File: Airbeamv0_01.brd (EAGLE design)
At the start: 91.4 x 74.3 mm, 89 parts

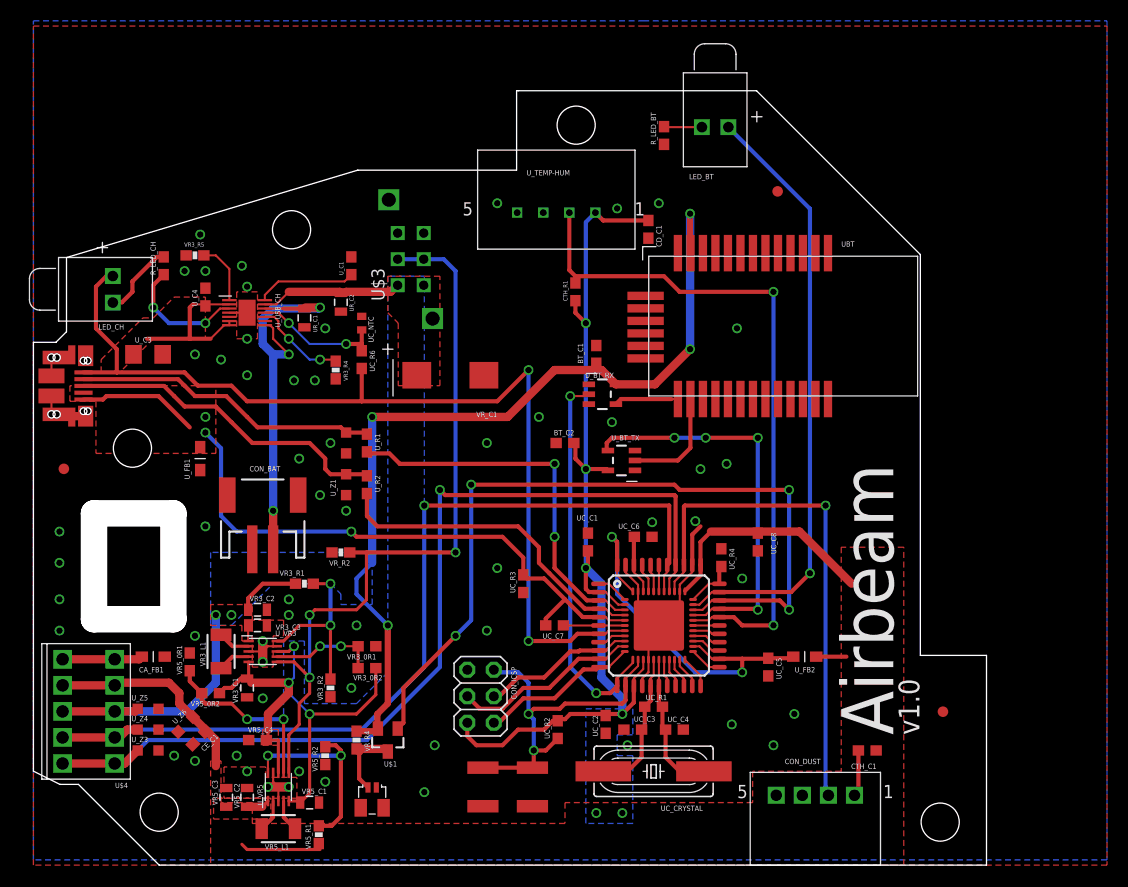
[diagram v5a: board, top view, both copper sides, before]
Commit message: updated bom, added ferrite bead
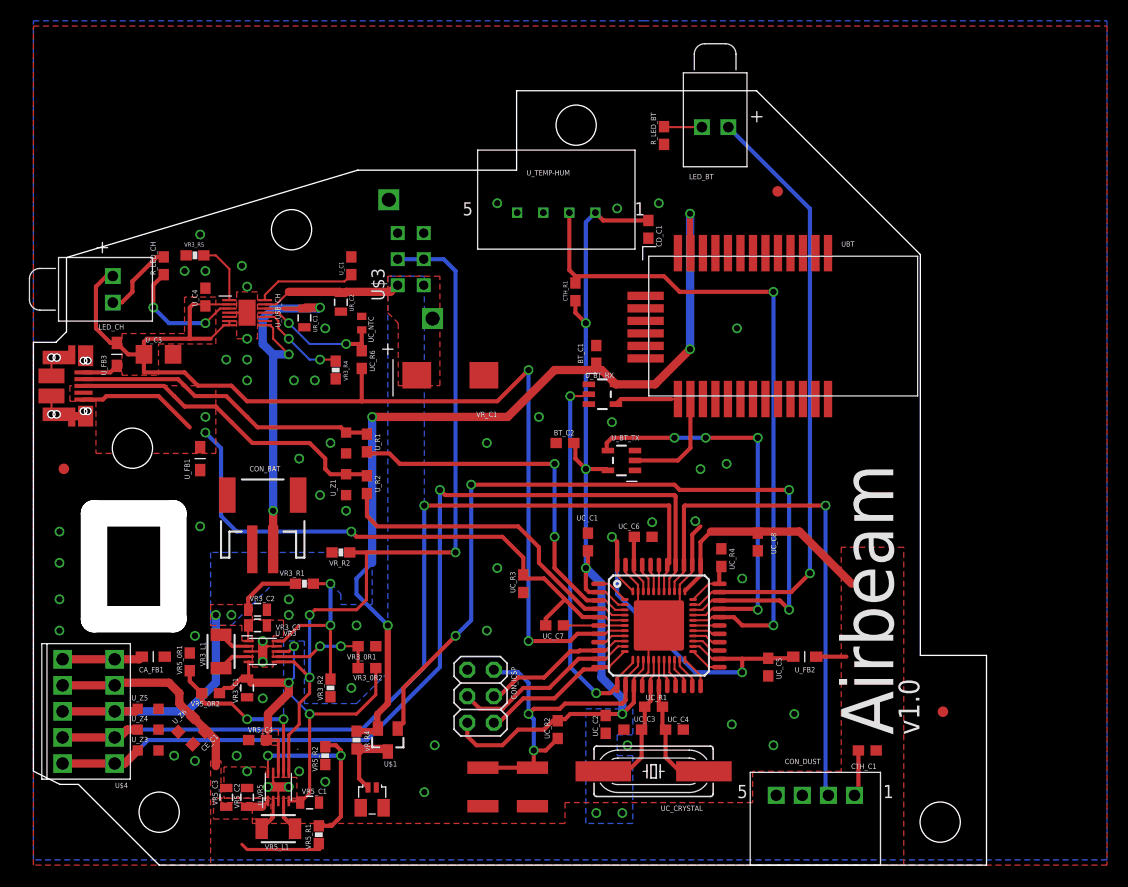
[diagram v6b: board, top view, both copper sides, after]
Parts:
- added U_FB3: FERITE_BEAD, Airbeam:U_FB1
- moved U_C3 1.00 mm to (12.0, 49.0)
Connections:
- new net VUSB: ATMEGA32U4-T.7, LED_CH.ANODE, UC_R6.2, U_C3.1, U_C4.1, U_FB3.P$2, U_MEGA32U-Q.7, U_USB_CH.P$2, U_USB_CH.P$6, U_USB_CH.P$7
- net XUSB: now also U_FB3.P$1; no longer ATMEGA32U4-T.7, LED_CH.ANODE, UC_R6.2, U_C3.1, U_C4.1, U_MEGA32U-Q.7, U_USB_CH.P$2, U_USB_CH.P$6, U_USB_CH.P$7
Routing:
- net VUSB: track 0.00 -> 108.9 mm, vias 0 -> 2
- net XUSB: track 110.8 -> 3.45 mm, vias 2 -> 0
- added copper zone on layer 1, net VUSB
- removed copper zone on layer 1, net XUSB
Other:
- outline, holes or cut-outs redrawn

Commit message: updating for ordering
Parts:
- RESET_SWITCH: value SWITCH -> DNP
- U_FANM: value MOSFET-N -> DNP
- renumbered U$1 to U_FANM, U$4 to CON_EXTERN
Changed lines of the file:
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@@
 <wire x1="5.768" y1="42.074" x2="5.768" y2="44.019" width="0.025" layer="49"/>
 <wire x1="5.768" y1="47.929" x2="5.768" y2="49.874" width="0.025" layer="49"/>
-<wire x1="46.53788125" y1="74.295" x2="46.53788125" y2="66.675" width="0.025" layer="49"/>
 <wire x1="3.358" y1="42.074" x2="4.058" y2="42.074" width="0.025" layer="49"/>
 <wire x1="4.308" y1="42.074" x2="5.768" y2="42.074" width="0.025" layer="49"/>
@@
 <wire x1="5.768" y1="49.874" x2="4.308" y2="49.874" width="0.025" layer="49"/>
 <wire x1="4.058" y1="49.874" x2="3.358" y2="49.874" width="0.025" layer="49"/>
-<wire x1="46.355" y1="66.675" x2="46.53788125" y2="66.675" width="0.025" layer="49"/>
 <wire x1="69.37761875" y1="74.295" x2="46.355" y2="74.295" width="0.025" layer="20"/>
 <circle x="9.525" y="40.005" radius="1.8288" width="0.025" layer="49"/>
@@
 <attribute name="NAME" x="45.847" y="19.021" size="0.508" layer="25" font="vector" ratio="27" rot="R270"/>
 <attribute name="PARTNO" value="67997-206HLF " x="42.9" y="16.2" size="1.778" layer="27" rot="R90" display="off"/>
-<attribute name="DNP" x="42.9" y="16.2" size="1.778" layer="27" rot="R90" display="off"/>
 </element>
 <element name="FID1" library="SmartPrj" package="FIDUCIA-MOUNT" value="FIDUCIALMOUNT" x="2.92" y="38.02" smashed="yes">
@@
 </element>
 <element name="ATMEGA32U4-T" library="SmartPrj" package="TQFP44-PAD" value="ATMEGA32U4-XUAU" x="60.01" y="22.99" smashed="yes">
-<attribute name="PARTNO" value="AtMega32U4-XUAU" x="60.01" y="22.99" size="1.778" layer="27" display="off"/>
+<attribute name="PARTNO" value="ATMEGA32U4-AU" x="60.01" y="22.99" size="1.778" layer="27" display="off"/>
 </element>
 <element name="UBT" library="Airbeam" package="BT_NVC-MDCS42A" value="BT-NVC-MDCS42A" x="76.2325" y="51.715" smashed="yes" rot="R270">
@@
 <attribute name="NAME" x="17.889" y="15.738" size="0.508" layer="25" font="vector" ratio="27" rot="R180"/>
 </element>
-<element name="RESET_SWITCH" library="Airbeam" package="SWITCH_TACTILE" value="SWITCH" x="45.5" y="7.5" smashed="yes" rot="R180">
+<element name="RESET_SWITCH" library="Airbeam" package="SWITCH_TACTILE" value="DNP" x="45.5" y="7.5" smashed="yes" rot="R180">
 <attribute name="PARTNO" value="TL3315NF250Q" x="45.5" y="7.5" size="1.778" layer="27" rot="R180" display="off"/>
 <attribute name="DNP" x="45.5" y="7.5" size="1.778" layer="27" rot="R180" display="off"/>
@@
 <attribute name="NAME" x="75" y="19" size="0.508" layer="25" ratio="27" rot="R180"/>
 </element>
-<element name="U$1" library="Airbeam" package="SOT23" value="MOSFET-N" x="34" y="12" smashed="yes" rot="R180">
+<element name="U_FANM" library="Airbeam" package="SOT23" value="DNP" x="34" y="12" smashed="yes" rot="R180">
 <attribute name="PARTNO" value="NDS331N" x="34" y="12" size="1.778" layer="27" rot="R180" display="off"/>
 <attribute name="NAME" x="34.889" y="9.968" size="0.508" layer="25" ratio="27" rot="R180"/>
@@
 <attribute name="PARTNO" value="RC0603JR-0710KL" x="52" y="55" size="0.508" layer="27" ratio="27" rot="R90" display="off"/>
 </element>
-<element name="U$4" library="Airbeam" package="TBLOCK_5" value="TBLOCK_5" x="5.3" y="14.75" locked="yes" rot="R90"/>
+<element name="CON_EXTERN" library="Airbeam" package="TBLOCK_5" value="TBLOCK_5" x="5.3" y="14.75" locked="yes" rot="R90">
+<attribute name="PARTNO" value="1770911" x="5.3" y="14.75" size="1.778" layer="27" font="vector" rot="R90" display="off"/>
+</element>
 <element name="U_FB3" library="Airbeam" package="U_FB1" value="FERITE_BEAD" x="8" y="49" smashed="yes" rot="R90">
 <attribute name="PARTNO" value="MH2029-600Y" x="8" y="49" size="1.778" layer="27" font="vector" rot="R90" display="off"/>
@@
 <wire x1="52" y1="53" x2="53" y2="52" width="0.4" layer="1"/>
 <via x="53" y="52" extent="1-16" drill="0.6" shape="square"/>
-<contactref element="U$4" pad="T_4"/>
-<contactref element="U$4" pad="B_4"/>
+<contactref element="CON_EXTERN" pad="T_4"/>
+<contactref element="CON_EXTERN" pad="B_4"/>
 <wire x1="53" y1="52" x2="53" y2="61.6833" width="0.4" layer="16"/>
 <wire x1="53" y1="61.6833" x2="53.915" y2="62.5983" width="0.4" layer="16"/>
@@
 <wire x1="61" y1="28.98" x2="60.81" y2="28.79" width="0.4064" layer="1"/>
 <contactref element="U_Z4" pad="1"/>
-<contactref element="U$4" pad="T_2"/>
-<contactref element="U$4" pad="B_2"/>
+<contactref element="CON_EXTERN" pad="T_2"/>
+<contactref element="CON_EXTERN" pad="B_2"/>
 <wire x1="2.8" y1="12.25" x2="7.8" y2="12.25" width="0.8" layer="1"/>
 <wire x1="7.8" y1="12.25" x2="8.25" y2="12.25" width="0.8" layer="1"/>
@@
 <wire x1="61.61" y1="35.39" x2="61.5" y2="35.5" width="0.4" layer="1"/>
 <contactref element="U_Z3" pad="1"/>
-<contactref element="U$4" pad="T_1"/>
-<contactref element="U$4" pad="B_1"/>
+<contactref element="CON_EXTERN" pad="T_1"/>
+<contactref element="CON_EXTERN" pad="B_1"/>
 <wire x1="2.8" y1="9.75" x2="7.8" y2="9.75" width="0.8" layer="1"/>
 <wire x1="7.8" y1="9.75" x2="8.75" y2="9.75" width="0.8" layer="1"/>
@@
 <wire x1="40.5" y1="22" x2="35.5" y2="17" width="0.4" layer="1"/>
 <wire x1="35.5" y1="17" x2="35.5" y2="13.65" width="0.4" layer="1"/>
-<contactref element="U$1" pad="1"/>
+<contactref element="U_FANM" pad="1"/>
 <wire x1="34.95" y1="13.1" x2="35.5" y2="13.65" width="0.4" layer="1"/>
 </signal>
@@
 <wire x1="20.6" y1="23" x2="20.6" y2="21.55" width="0.2" layer="1"/>
 <wire x1="20.6" y1="21.55" x2="20.65" y2="21.5" width="0.2" layer="1"/>
-<contactref element="U$1" pad="2"/>
+<contactref element="U_FANM" pad="2"/>
 <wire x1="33" y1="13.15" x2="33.05" y2="13.1" width="0.4" layer="1"/>
 <wire x1="33.05" y1="13.1" x2="32.8" y2="12.85" width="0.4" layer="1"/>
-<contactref element="U$4" pad="T_3"/>
-<contactref element="U$4" pad="B_3"/>
+<contactref element="CON_EXTERN" pad="T_3"/>
+<contactref element="CON_EXTERN" pad="B_3"/>
 <wire x1="7.8" y1="14.75" x2="2.8" y2="14.75" width="0.8" layer="1"/>
 <wire x1="14.75" y1="14.75" x2="17.5" y2="17.5" width="0.8" layer="16"/>
@@
 <wire x1="31" y1="11.15" x2="33.75" y2="11.15" width="0.8" layer="1"/>
 <wire x1="31.24995" y1="10.90005" x2="31" y2="11.15" width="0.8" layer="1"/>
-<contactref element="U$1" pad="3"/>
+<contactref element="U_FANM" pad="3"/>
 <wire x1="33.75" y1="11.15" x2="34" y2="10.9" width="0.4" layer="1"/>
 <contactref element="U$2" pad="P1"/>
@@
 <signal name="N$7" class="2">
 <contactref element="CA_FB1" pad="P$2"/>
-<contactref element="U$4" pad="T_5"/>
-<contactref element="U$4" pad="B_5"/>
+<contactref element="CON_EXTERN" pad="T_5"/>
+<contactref element="CON_EXTERN" pad="B_5"/>
 <wire x1="7.8" y1="19.75" x2="2.8" y2="19.75" width="0.8" layer="1"/>
 <wire x1="7.8" y1="19.75" x2="10.15" y2="19.75" width="0.8" layer="1"/>

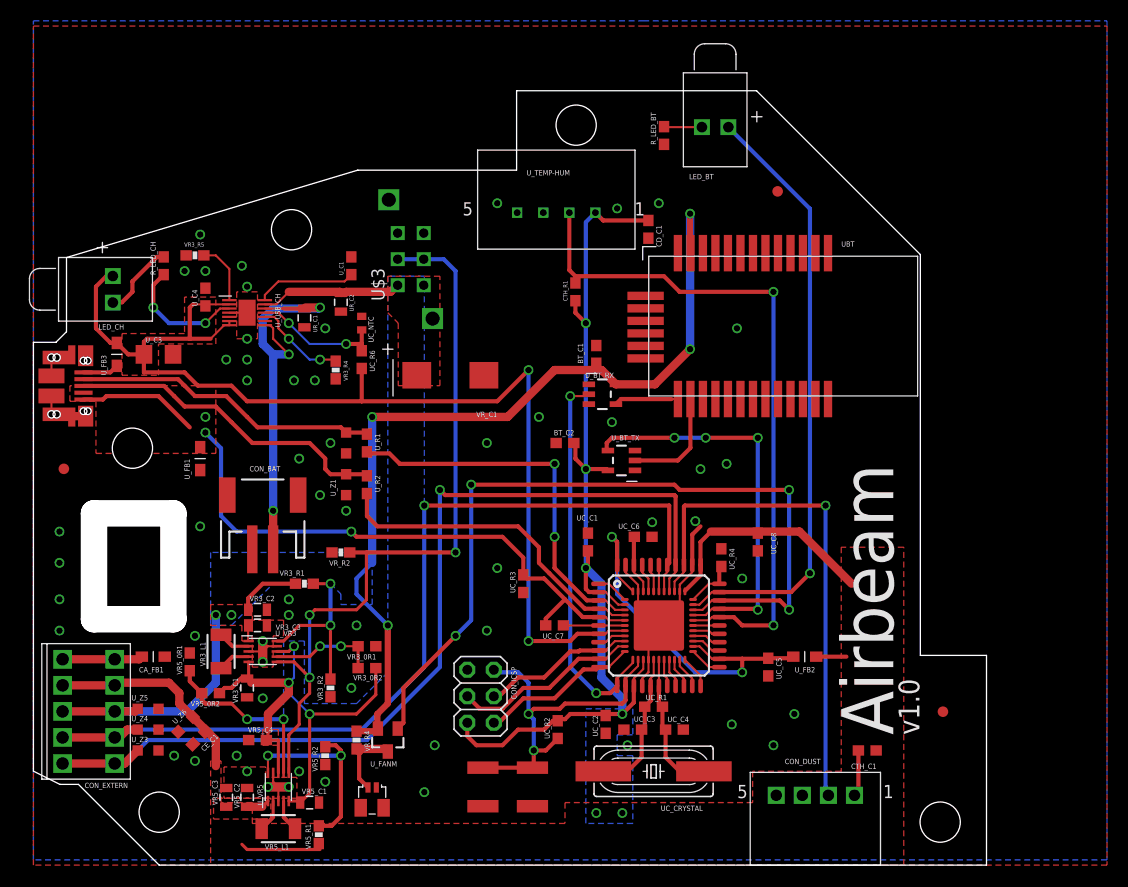
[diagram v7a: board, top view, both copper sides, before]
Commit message: BOM updated, board outline modified for cheaper version (per Chris), FINAL
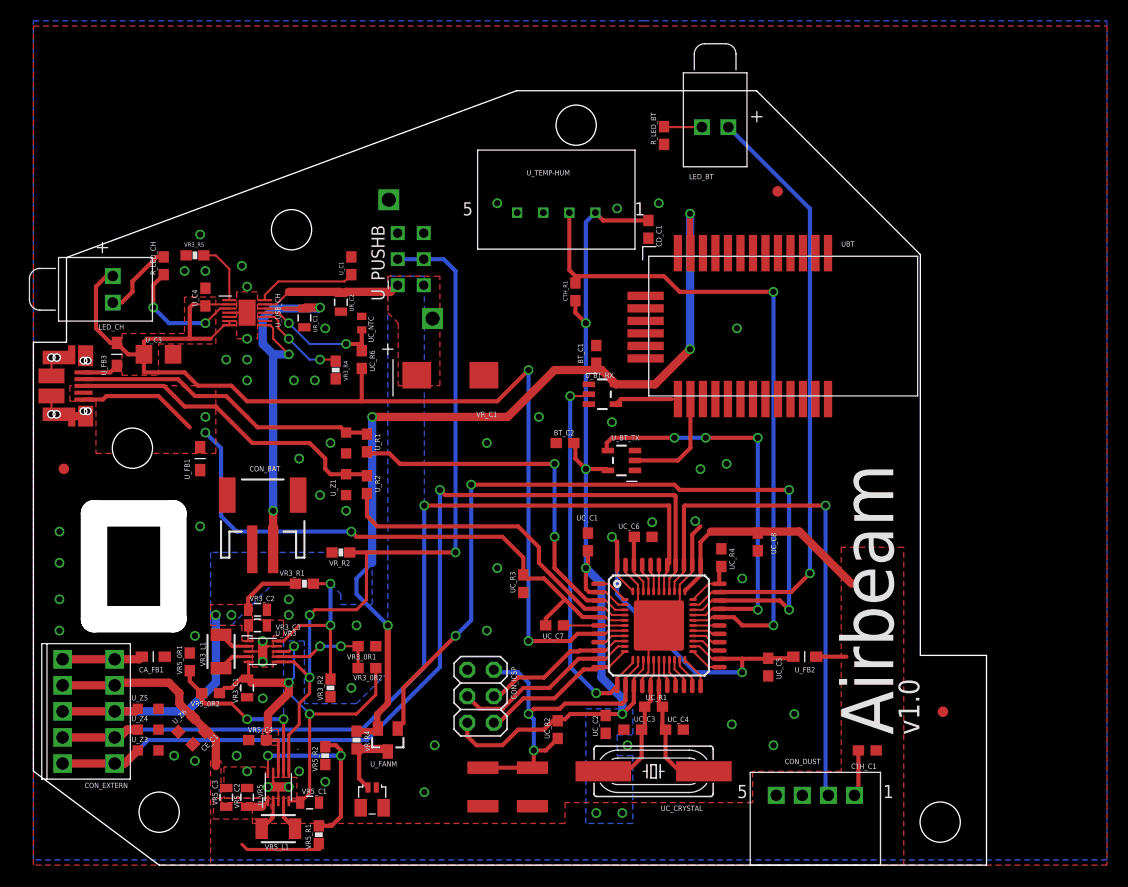
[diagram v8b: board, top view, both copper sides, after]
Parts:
- renumbered U$2 to CON_FAN, U$3 to U_PUSHB
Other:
- outline, holes or cut-outs redrawn
